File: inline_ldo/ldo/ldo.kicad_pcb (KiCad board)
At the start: 4 copper layers, 22.1 x 15.2 mm, 11 parts, among them J2 USB_A, U2 LT3045xDD

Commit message: almost finished hopefully
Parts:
- added TP1: TestPoint, TestPoint:TestPoint_Pad_D1.0mm, F.Cu at (48.8, 71.4)
- added TP2: TestPoint, TestPoint:TestPoint_Pad_D1.0mm, F.Cu at (54.4, 71.4)
- moved C5 2.18 mm to (54.4, 70.1), turned to 0 degrees
- moved C1 0.76 mm to (48.7, 67.8)
- moved R6 0.25 mm to (52.3, 70.1)
- turned C2 to -90 degrees
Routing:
- net VIN: track 0.00 -> 26.3 mm, vias 0 -> 3
- net 5V: track 0.00 -> 12.1 mm
- net GND: track 0.00 -> 3.79 mm, vias 0 -> 3
- net Net-(U2-SET): track 0.00 -> 3.44 mm
- net Net-(J1-SHIELD): track 20.9 -> 23.4 mm, vias 0 -> 2
- net /USB_CC2: track 11.3 -> 12.7 mm
- added copper zone on B.Cu, net GND
- added copper zone on F.Cu, net GND
- added copper zone on In1.Cu, net GND
- added copper zone on In2.Cu, net GND

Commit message: pushes
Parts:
- removed TP1, TP2: TestPoint, TestPoint:TestPoint_Pad_D1.0mm
- added D1: SBR3U60P1-7, Diode_SMD:D_PowerDI-123, B.Cu at (51.8, 66.7)
- added R7: 1M, Capacitor_SMD:C_0402_1005Metric, F.Cu at (49.4, 59.1)
- added R8: 1M, Capacitor_SMD:C_0402_1005Metric, F.Cu at (54.5, 60.1)
- moved R1 2.69 mm to (49.4, 61.1)
- moved C4 2.16 mm to (54.5, 59.1)
- moved C1 2.12 mm to (48.7, 69.9)
- moved C2 2.12 mm to (54.6, 69.9)
- moved C5 2.12 mm to (54.3, 72.2)
- moved R6 2.12 mm to (52.3, 72.2)
- moved U2 2.12 mm to (51.6, 69.8)
- moved C3 1.20 mm to (49.4, 60.1)
- moved R2 0.54 mm to (49.4, 62.1)
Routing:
- net VIN: track 26.3 -> 21.4 mm, vias 3 -> 2
- net /USB_CC2: track 12.7 -> 8.43 mm
- net GND: track 3.79 -> 7.82 mm, vias 3 -> 53
- net 5V: track 12.1 -> 8.96 mm, vias 0 -> 1
- net /USB_CC1: track 1.89 -> 4.26 mm
- net /D-: track 11.2 -> 13.5 mm, vias 2 -> 0
- net Net-(J1-SHIELD): track 23.4 -> 21.9 mm, vias 2 -> 0
- net /D+: track 11.5 -> 13.0 mm

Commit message: need to redo vias
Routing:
- net GND: track 7.82 -> 19.4 mm, vias 53 -> 71
- net /D+: track 13.0 -> 14.6 mm
- net /D-: track 13.5 -> 12.4 mm
- net /USB_CC2: track 8.43 -> 7.36 mm
- net VIN: track 21.4 -> 20.7 mm
- net 5V: track 8.96 -> 9.56 mm
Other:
- board text added: "{ "ViaStitching": "0.2", "stitch_zone_0": { "HSpacing": "1", "VSpacing": "1", "HOffset": "0", "VOffset": "0", "Clearance": "0", "Randomize": false } }"
- board text added: "{ "ViaStitching": "0.2", "stitch_zone_0": { "HSpacing": "1.5", "VSpacing": "1.5", "HOffset": "0", "VOffset": "0", "Clearance": "0", "Randomize": false } }"
- board text added: "{ "ViaStitching": "0.2", "stitch_zone_0": { "HSpacing": "2.5", "VSpacing": "2.5", "HOffset": "0", "VOffset": "0", "Clearance": "0", "Randomize": false } }"
- board text added: "{ "ViaStitching": "0.2", "stitch_zone_0": { "HSpacing": "3", "VSpacing": "3", "HOffset": "0", "VOffset": "0", "Clearance": "0", "Randomize": false } }"

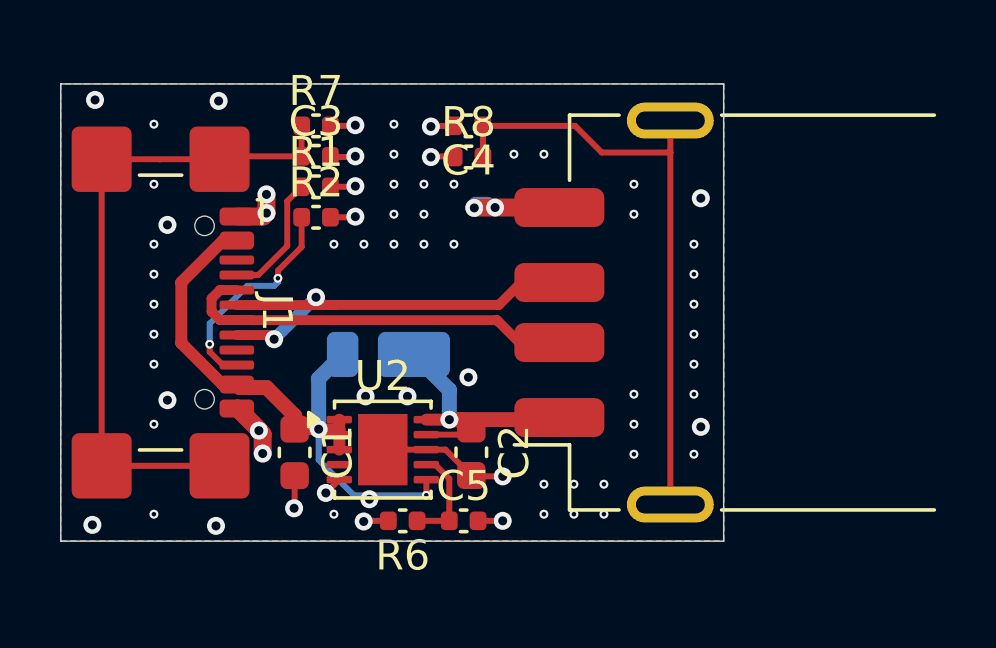
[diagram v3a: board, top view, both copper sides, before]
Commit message: fixed most via sizing issues
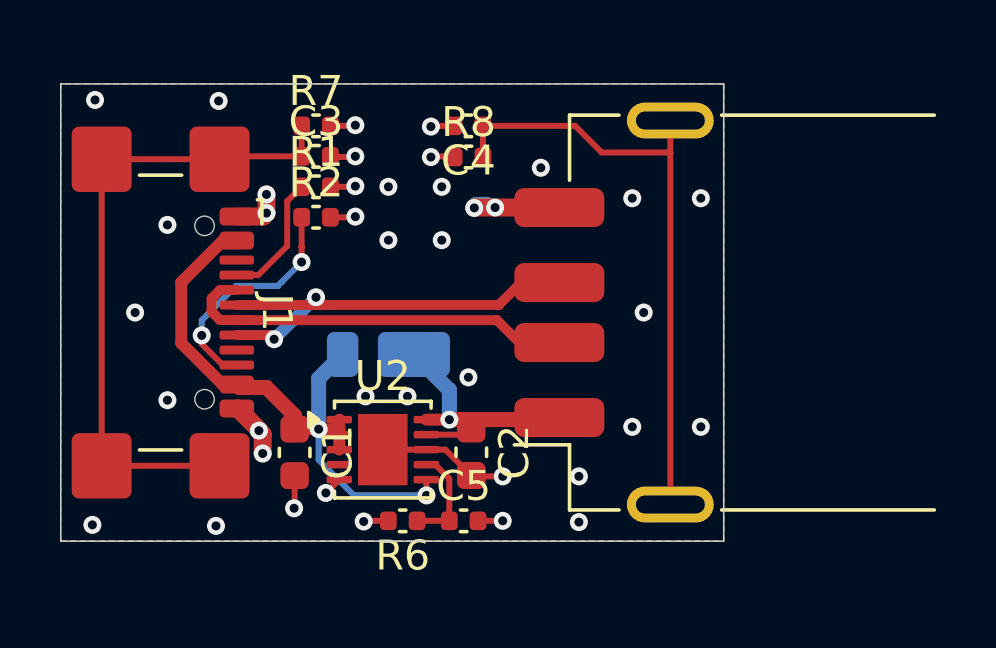
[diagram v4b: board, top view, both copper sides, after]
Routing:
- net /USB_CC2: track 7.36 -> 7.91 mm
- net GND: vias 71 -> 39
